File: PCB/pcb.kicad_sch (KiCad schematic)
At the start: 173 parts, among them J1 EXT POWER, J2 TRACK POWER, J3 RJ45, J4 RJ45, J5 FROG0-1, J6 FROG2-3, J7 FROG4-5, J8 FROG6-7, K1 G6SK-2, K2 G6SK-2, K3 G6SK-2, K4 G6SK-2, K5 G6SK-2, K6 G6SK-2, K7 G6SK-2, K8 G6SK-2, M1 Motor_Servo, M2 Motor_Servo, M3 Motor_Servo, M4 Motor_Servo, M5 Motor_Servo, M6 Motor_Servo, M7 Motor_Servo, M8 Motor_Servo, Q1 MMBT2222A, Q10 MMBT2222A, Q11 MMBT2222A, Q12 MMBT2222A, Q13 MMBT2222A, Q14 MMBT2222A, Q15 MMBT2222A, Q16 MMBT2222A, Q2 MMBT2222A, Q3 MMBT2222A, Q4 MMBT2222A, Q5 MMBT2222A, Q6 MMBT2222A, Q7 MMBT2222A, Q8 MMBT2222A, Q9 MMBT2222A, SW2 Factory Reset, SW3 User, U2 PCA9685PW, U3 MCP23017_SO, U4 AP63205WU, U5 AP2114-3.3, U6 LM358, U7 TJA1051T-3, U8 MOUDLE-SEEEDUINO-XIAO-ESP32S3

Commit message: Update with XIAO footprint
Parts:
- U8: footprint xiao ESP32S3_PCB:MOUDLE14P-SMD-2.54-21X17.8MM -> CustomFootprints:MCU_Seeed_ESP32C3_TH
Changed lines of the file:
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@@
 			)
 		)
-		(property "Footprint" "xiao ESP32S3_PCB:MOUDLE14P-SMD-2.54-21X17.8MM"
+		(property "Footprint" "CustomFootprints:MCU_Seeed_ESP32C3_TH"
 			(at 69.85 52.07 0)
 			(effects

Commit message: Update project files
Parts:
- added D1: WiFi, LED_SMD:LED_0603_1608Metric, symbol Device:LED_Small
- added D2: Activity, LED_SMD:LED_0603_1608Metric, symbol Device:LED_Small
- added R10, R11: 220R, Resistor_SMD:R_0603_1608Metric, symbol Device:R_Small
- H1, H2, H3, H4: footprint MountingHole:MountingHole_2.7mm_M2.5 -> MountingHole:MountingHole_3.2mm_M3_Pad
- SW2, SW3: footprint Button_Switch_SMD:SW_SPST_EVQPE1 -> Button_Switch_SMD:SW_Tactile_SPST_NO_Straight_CK_PTS636Sx25SMTRLFS
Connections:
- net +3V3: now also D1.2 (A), D2.2 (A)
- net CAN-RX: now also U8.9 (PA7_A8_D8_SCK); no longer U8.10 (PA5_A9_D9_MISO)
- net CAN-TX: now also U8.10 (PA5_A9_D9_MISO); no longer U8.11 (PA6_A10_D10_MOSI)
- net FACTORY_RESET: now also U8.3 (PA10_A2_D2); no longer U8.2 (PA4_A1_D1)
- net GPIO_nRESET: no longer U8.3 (PA10_A2_D2)
- net USER_BTN: now also U8.2 (PA4_A1_D1); no longer U8.1 (PA02_A0_D0)
- new net: D2.1 (K), R11.2
- new net: D1.1 (K), R10.2
- new net ACTIVITY_LED: R11.1, U8.11 (PA6_A10_D10_MOSI)
- new net WIFI_LED: R10.1, U8.1 (PA02_A0_D0)
- no-connect marks 12 -> 11

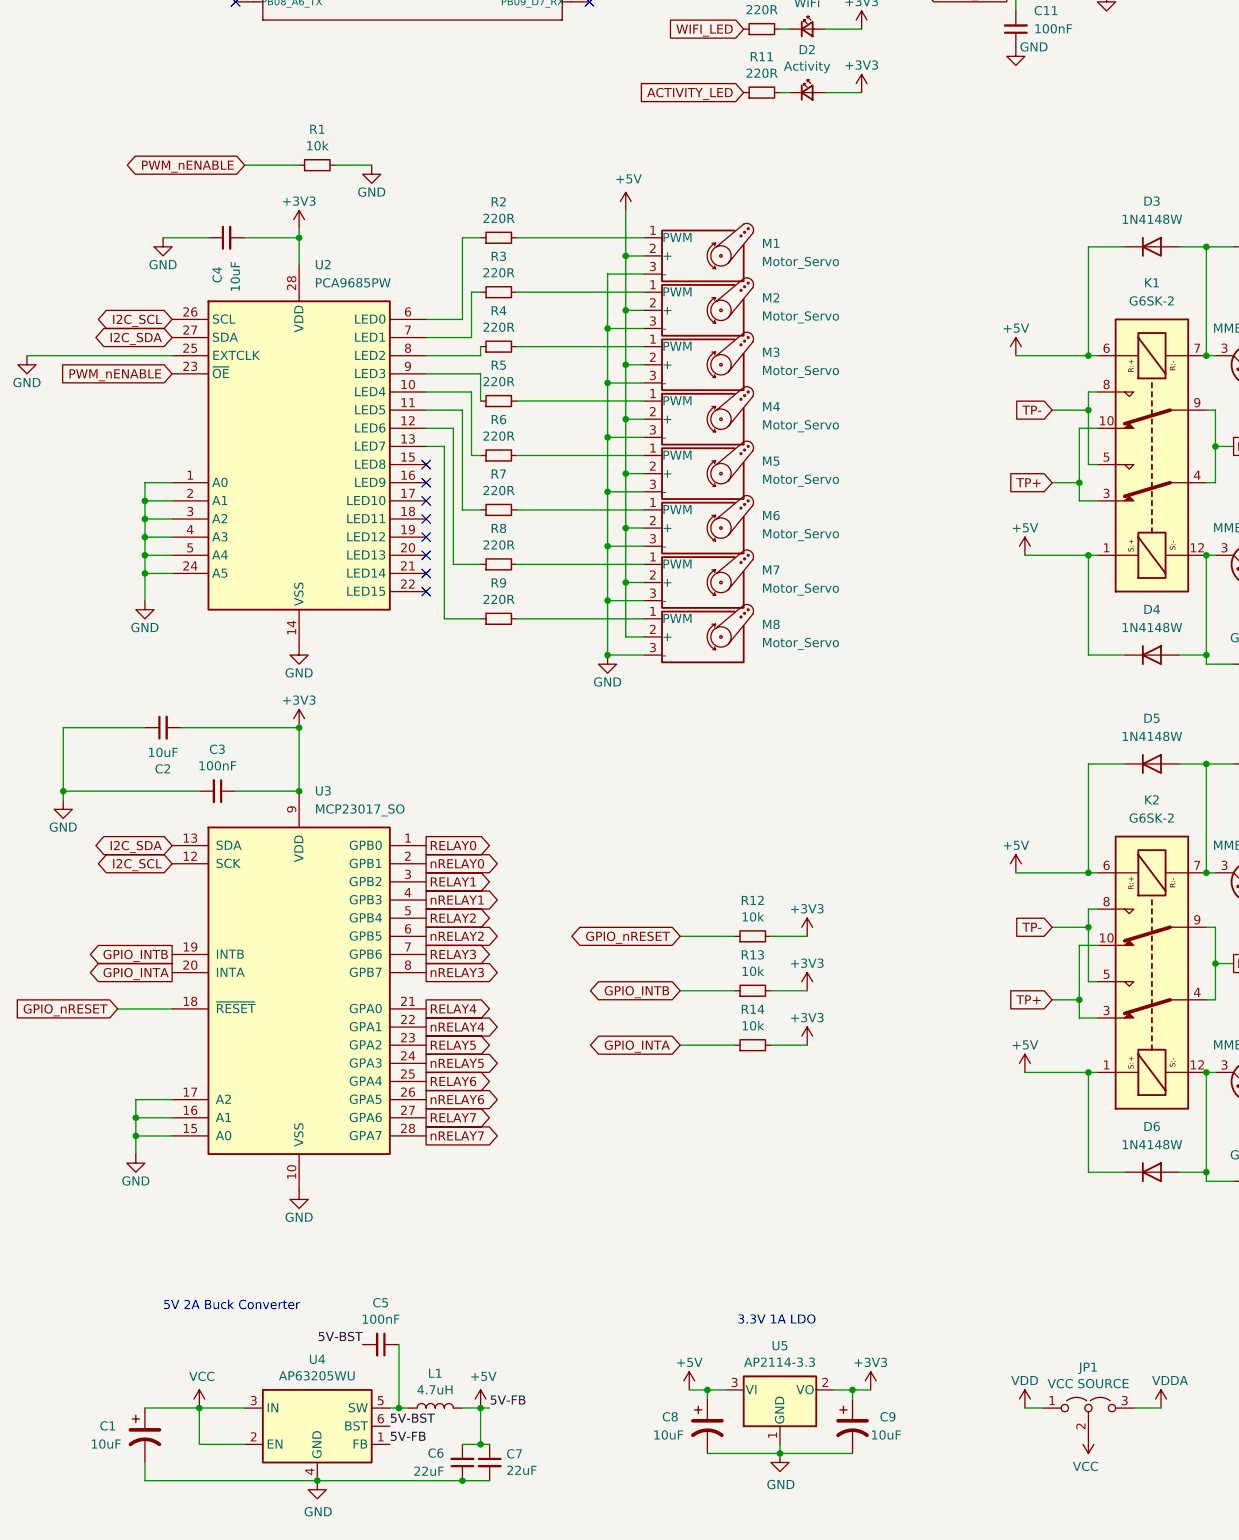
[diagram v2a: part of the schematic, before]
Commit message: Fix live config updates not taking effect until reboot
ServoTurnout: preserve current state across ServoGPIOBit reconstruction
during runtime config changes. Previously, the placement-new reset
currentState_ to false, causing the first toggle to be silently eaten
(early return in set_state) and leaving the servo at stale endpoints.

Now saves the logical state before reconstruction and immediately
re-applies it via restore_state() with the new endpoint/frog values.
Also adds diagnostic logging to apply_configuration.

Includes PCB design updates.
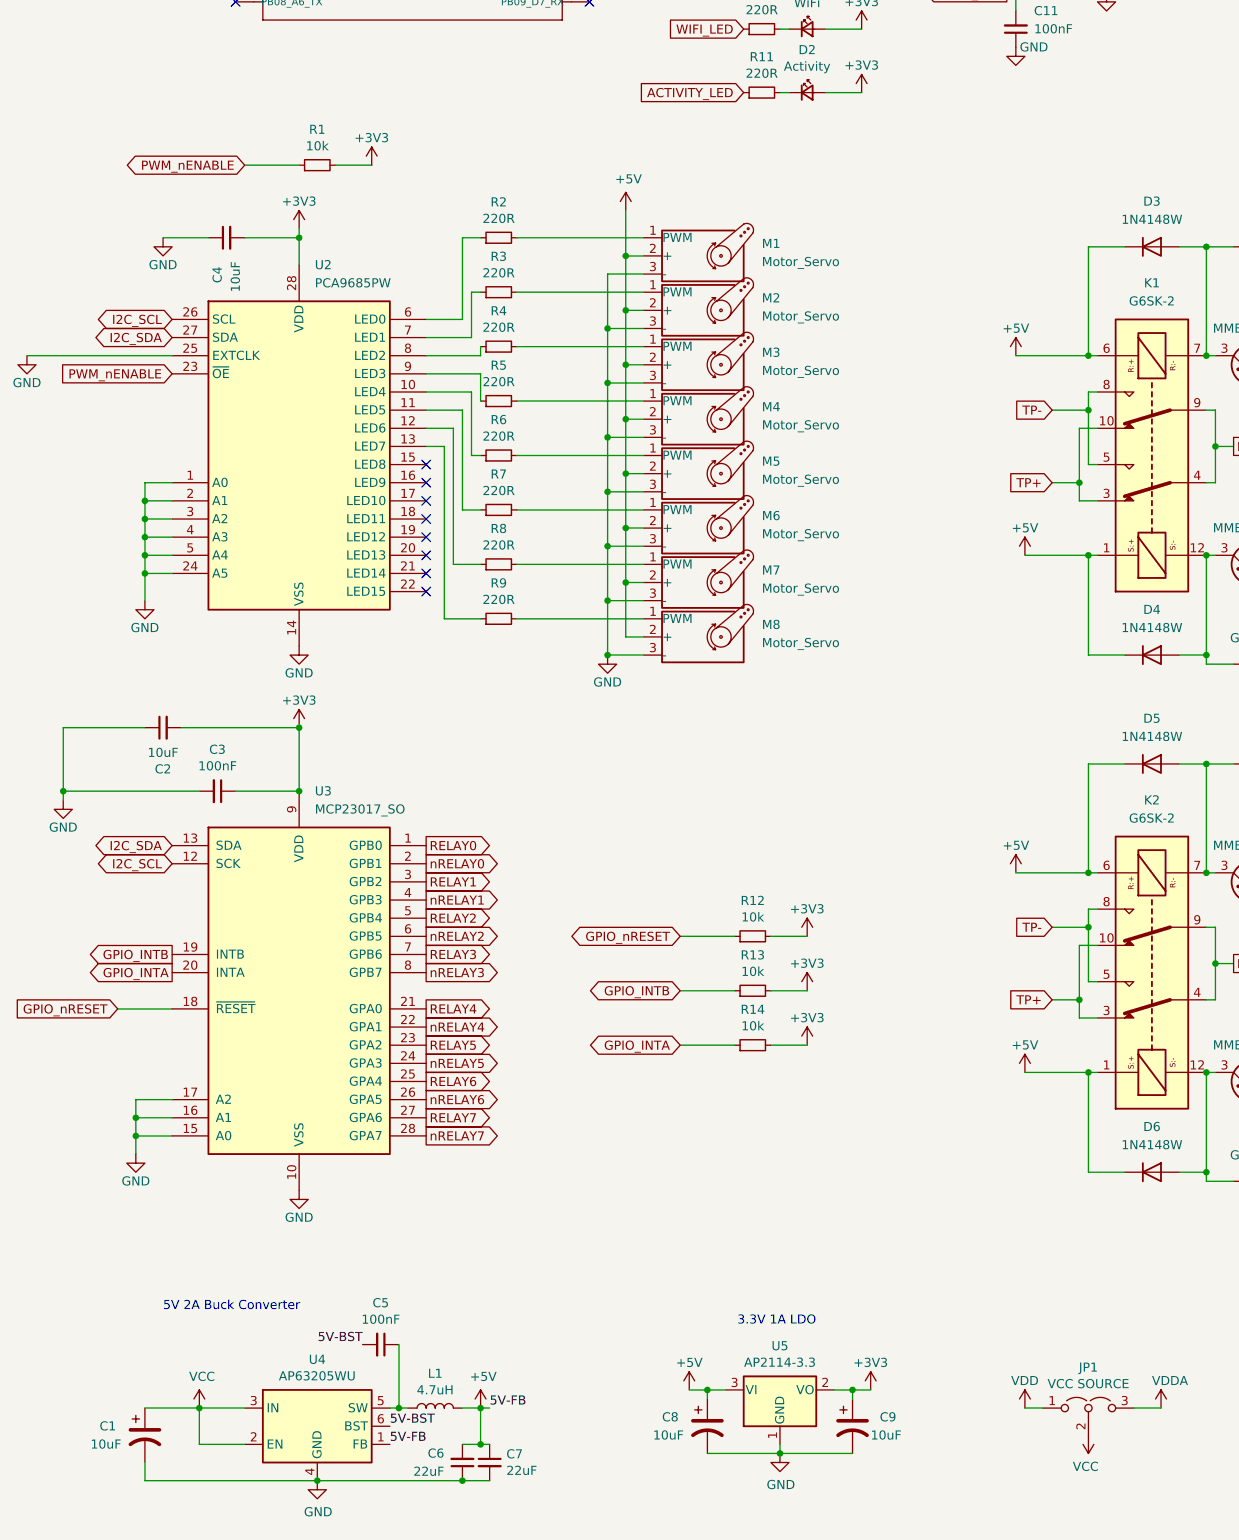
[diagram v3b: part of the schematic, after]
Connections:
- net +3V3: now also R1.2
- net GND: no longer R1.2
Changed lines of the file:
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@@
 (kicad_sch
-	(version 20231120)
+	(version 20250114)
 	(generator "eeschema")
-	(generator_version "8.0")
+	(generator_version "9.0")
 	(paper "A3")
 	(title_block
@@
 		(rev "1.0")
 	)
+	(text "I2C Pullup Resistors"
+		(exclude_from_sim no)
+		(at 210.312 17.272 0)
+		(effects
+			(font
+				(size 1.27 1.27)
+			)
+			(justify right bottom)
+		)
+	)
+	(text "5V 2A Buck Converter"
+		(exclude_from_sim no)
+		(at 34.29 246.888 0)
+		(effects
+			(font
+				(size 1.27 1.27)
+			)
+			(justify left bottom)
+		)
+	)
+	(text "3.3V 1A LDO"
+		(exclude_from_sim no)
+		(at 125.73 248.92 0)
+		(effects
+			(font
+				(size 1.27 1.27)
+			)
+			(justify right bottom)
+		)
+	)
+	(text "ESP32 DevKit-C or TTGO-T1 Module"
+		(exclude_from_sim no)
+		(at 52.07 29.21 0)
+		(effects
+			(font
+				(size 1.27 1.27)
+			)
+			(justify left bottom)
+		)
+	)
+	(text "CAN Transceiver with split voltage"
+		(exclude_from_sim no)
+		(at 353.06 19.05 0)
+		(effects
+			(font
+				(size 1.27 1.27)
+			)
+			(justify right bottom)
+		)
+	)
+	(text "CAN Activity LEDs"
+		(exclude_from_sim no)
+		(at 278.13 16.51 0)
+		(effects
+			(font
+				(size 1.27 1.27)
+			)
+			(justify left bottom)
+		)
+	)
+	(text "Dual line TVS for CAN Bus H/L"
+		(exclude_from_sim no)
+		(at 260.35 16.51 0)
+		(effects
+			(font
+				(size 1.27 1.27)
+			)
+			(justify right bottom)
+		)
+	)
 	(junction
 		(at 256.54 193.04)
@@
 		)
 	)
-	(text "I2C Pullup Resistors"
-		(exclude_from_sim no)
-		(at 210.312 17.272 0)
-		(effects
-			(font
-				(size 1.27 1.27)
-			)
-			(justify right bottom)
-		)
-	)
-	(text "5V 2A Buck Converter"
-		(exclude_from_sim no)
-		(at 34.29 246.888 0)
-		(effects
-			(font
-				(size 1.27 1.27)
-			)
-			(justify left bottom)
-		)
-	)
-	(text "3.3V 1A LDO"
-		(exclude_from_sim no)
-		(at 125.73 248.92 0)
-		(effects
-			(font
-				(size 1.27 1.27)
-			)
-			(justify right bottom)
-		)
-	)
-	(text "ESP32 DevKit-C or TTGO-T1 Module"
-		(exclude_from_sim no)
-		(at 52.07 29.21 0)
-		(effects
-			(font
-				(size 1.27 1.27)
-			)
-			(justify left bottom)
-		)
-	)
-	(text "CAN Transceiver with split voltage"
-		(exclude_from_sim no)
-		(at 353.06 19.05 0)
-		(effects
-			(font
-				(size 1.27 1.27)
-			)
-			(justify right bottom)
-		)
-	)
-	(text "CAN Activity LEDs"
-		(exclude_from_sim no)
-		(at 278.13 16.51 0)
-		(effects
-			(font
-				(size 1.27 1.27)
-			)
-			(justify left bottom)
-		)
-	)
-	(text "Dual line TVS for CAN Bus H/L"
-		(exclude_from_sim no)
-		(at 260.35 16.51 0)
-		(effects
-			(font
-				(size 1.27 1.27)
-			)
-			(justify right bottom)
-		)
-	)
 	(label "5V-FB"
 		(at 66.04 265.43 0)
-		(fields_autoplaced yes)
 		(effects
 			(font
@@
 	(label "5V-BST"
 		(at 66.04 262.89 0)
-		(fields_autoplaced yes)
 		(effects
 			(font
@@
 	(label "5V-BST"
 		(at 62.23 251.46 180)
-		(fields_autoplaced yes)
 		(effects
 			(font
@@
 	(label "5V-FB"
 		(at 80.01 260.35 0)
-		(fields_autoplaced yes)
 		(effects
 			(font
@@
 	)
 	(symbol
+		(lib_id "power:+3V3")
+		(at 63.5 86.36 0)
+		(unit 1)
+		(exclude_from_sim no)
+		(in_bom yes)
+		(on_board yes)
+		(dnp no)
+		(property "Reference" "#PWR014"
+			(at 63.5 90.17 0)
+			(effects
+				(font
+					(size 1.27 1.27)
+				)
+				(hide yes)
+			)
+		)
+		(property "Value" "+3V3"
+			(at 63.5 82.55 0)
+			(effects
+				(font
+					(size 1.27 1.27)
+				)
+			)
+		)
+		(property "Footprint" ""
+			(at 63.5 86.36 0)
+			(effects
+				(font
+					(size 1.27 1.27)
+				)
+				(hide yes)
+			)
+		)
+		(property "Datasheet" ""
+			(at 63.5 86.36 0)
+			(effects
+				(font
+					(size 1.27 1.27)
+				)
+				(hide yes)
+			)
+		)
+		(property "Description" ""
+			(at 63.5 86.36 0)
+			(effects
+				(font
+					(size 1.27 1.27)
+				)
+				(hide yes)
+			)
+		)
+		(pin "1"
+		)
+		(instances
+			(project "pcb"
+				(path "/4431c0f6-83ea-4eee-95a8-991da2f03ccd"
+					(reference "#PWR014")
+					(unit 1)
+				)
+			)
+		)
+	)
+	(symbol
 		(lib_id "Device:R_Small")
 		(at 384.81 116.84 0)
@@
 	)
 	(symbol
-		(lib_id "power:GND")
-		(at 63.5 86.36 0)
-		(unit 1)
-		(exclude_from_sim no)
-		(in_bom yes)
-		(on_board yes)
-		(dnp no)
-		(property "Reference" "#PWR014"
-			(at 63.5 92.71 0)
-			(effects
-				(font
-					(size 1.27 1.27)
-				)
-				(hide yes)
-			)
-		)
-		(property "Value" "GND"
-			(at 63.5 90.17 0)
-			(effects
-				(font
-					(size 1.27 1.27)
-				)
-			)
-		)
-		(property "Footprint" ""
-			(at 63.5 86.36 0)
-			(effects
-				(font
-					(size 1.27 1.27)
-				)
-				(hide yes)
-			)
-		)
-		(property "Datasheet" ""
-			(at 63.5 86.36 0)
-			(effects
-				(font
-					(size 1.27 1.27)
-				)
-				(hide yes)
-			)
-		)
-		(property "Description" ""
-			(at 63.5 86.36 0)
-			(effects
-				(font
-					(size 1.27 1.27)
-				)
-				(hide yes)
-			)
-		)
-		(pin "1"
-		)
-		(instances
-			(project "pcb"
-				(path "/4431c0f6-83ea-4eee-95a8-991da2f03ccd"
-					(reference "#PWR014")
-					(unit 1)
-				)
-			)
-		)
-	)
-	(symbol
 		(lib_id "Device:LED_Small")
 		(at 250.19 170.18 0)
@@
 		)
 	)
+	(embedded_fonts no)
 )
